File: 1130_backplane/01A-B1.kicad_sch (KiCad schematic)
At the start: 86 parts

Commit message: DN101-DN111 added to backplane schematics, DN111 01B-A1 connections made, 01B-B1 connections to be made when all signals on connectors
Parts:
- removed J100, J101, J102, J103, J104, J105, J106, J107, J108, J109, J110, J111, J112, J113, J114, J115, J116, J117, J118, J119, J120, J121, J122, J123, J124, J125, J126, J127, J128, J129, J130, J131, J132, J133, J134, J135, J136, J137, J138, J139, J140, J141, J142, J143, J144, J145, J146, J147, J148, J149, J150, J151, J152, J153, J154, J155, J156, J157, J158, J159, J160, J161, J162, J163, J164, J165, J166, J167, J168, J169, J170, J171, J172, J87, J88, J89, J90, J91, J92, J93, J94, J95, J96, J97, J98, J99: ~, symbol Connector_Generic:Conn_02x12_Row_Letter_First
- added J? (x86): ~, symbol Connector_Generic:Conn_02x12_Row_Letter_First
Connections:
- net +3V: now also J?.b2 (Pin_b2), J?.b2 (Pin_b2), J?.b2 (Pin_b2), J?.b2 (Pin_b2), J?.b2 (Pin_b2), J?.b2 (Pin_b2), J?.b2 (Pin_b2), J?.b2 (Pin_b2), J?.b2 (Pin_b2), J?.b2 (Pin_b2), J?.b2 (Pin_b2), J?.b2 (Pin_b2), J?.b2 (Pin_b2), J?.b2 (Pin_b2), J?.b2 (Pin_b2), J?.b2 (Pin_b2), J?.b2 (Pin_b2), J?.b2 (Pin_b2), J?.b2 (Pin_b2), J?.b2 (Pin_b2), J?.b2 (Pin_b2), J?.b2 (Pin_b2), J?.b2 (Pin_b2), J?.b2 (Pin_b2), J?.b2 (Pin_b2), J?.b2 (Pin_b2), J?.b2 (Pin_b2), J?.b2 (Pin_b2), J?.b2 (Pin_b2), J?.b2 (Pin_b2), J?.b2 (Pin_b2), J?.b2 (Pin_b2), J?.b2 (Pin_b2), J?.b2 (Pin_b2), J?.b2 (Pin_b2), J?.b2 (Pin_b2), J?.b2 (Pin_b2), J?.b2 (Pin_b2), J?.b2 (Pin_b2), J?.b2 (Pin_b2), J?.b2 (Pin_b2), J?.b2 (Pin_b2), J?.b2 (Pin_b2), J?.b2 (Pin_b2), J?.b2 (Pin_b2), J?.b2 (Pin_b2), J?.b2 (Pin_b2), J?.b2 (Pin_b2), J?.b2 (Pin_b2), J?.b2 (Pin_b2), J?.b2 (Pin_b2), J?.b2 (Pin_b2), J?.b2 (Pin_b2), J?.b2 (Pin_b2), J?.b2 (Pin_b2), J?.b2 (Pin_b2), J?.b2 (Pin_b2), J?.b2 (Pin_b2), J?.b2 (Pin_b2), J?.b2 (Pin_b2), J?.b2 (Pin_b2), J?.b2 (Pin_b2), J?.b2 (Pin_b2), J?.b2 (Pin_b2), J?.b2 (Pin_b2), J?.b2 (Pin_b2), J?.b2 (Pin_b2), J?.b2 (Pin_b2), J?.b2 (Pin_b2), J?.b2 (Pin_b2), J?.b2 (Pin_b2), J?.b2 (Pin_b2), J?.b2 (Pin_b2), J?.b2 (Pin_b2), J?.b2 (Pin_b2), J?.b2 (Pin_b2), J?.b2 (Pin_b2)
- net +6V: now also J?.a10 (Pin_a10), J?.a10 (Pin_a10), J?.a10 (Pin_a10), J?.a10 (Pin_a10), J?.a10 (Pin_a10), J?.a10 (Pin_a10), J?.a10 (Pin_a10), J?.a10 (Pin_a10), J?.a10 (Pin_a10), J?.a10 (Pin_a10), J?.a10 (Pin_a10), J?.a10 (Pin_a10), J?.a10 (Pin_a10), J?.a10 (Pin_a10), J?.a10 (Pin_a10), J?.a10 (Pin_a10), J?.a10 (Pin_a10), J?.a10 (Pin_a10), J?.a10 (Pin_a10), J?.a10 (Pin_a10), J?.a10 (Pin_a10), J?.a10 (Pin_a10), J?.a10 (Pin_a10), J?.a10 (Pin_a10), J?.a10 (Pin_a10), J?.a10 (Pin_a10), J?.a10 (Pin_a10), J?.a10 (Pin_a10), J?.a10 (Pin_a10), J?.a10 (Pin_a10), J?.a10 (Pin_a10), J?.a10 (Pin_a10), J?.a10 (Pin_a10), J?.a10 (Pin_a10), J?.a10 (Pin_a10), J?.a10 (Pin_a10), J?.a10 (Pin_a10), J?.a10 (Pin_a10), J?.a10 (Pin_a10), J?.a10 (Pin_a10), J?.a10 (Pin_a10), J?.a10 (Pin_a10), J?.a10 (Pin_a10), J?.a10 (Pin_a10), J?.a10 (Pin_a10), J?.a10 (Pin_a10), J?.a10 (Pin_a10), J?.a10 (Pin_a10), J?.a10 (Pin_a10), J?.a10 (Pin_a10), J?.a10 (Pin_a10), J?.a10 (Pin_a10), J?.a10 (Pin_a10), J?.a10 (Pin_a10), J?.a10 (Pin_a10), J?.a10 (Pin_a10), J?.a10 (Pin_a10), J?.a10 (Pin_a10), J?.a10 (Pin_a10), J?.a10 (Pin_a10), J?.a10 (Pin_a10), J?.a10 (Pin_a10), J?.a10 (Pin_a10), J?.a10 (Pin_a10), J?.a10 (Pin_a10), J?.a10 (Pin_a10), J?.a10 (Pin_a10), J?.a10 (Pin_a10), J?.a10 (Pin_a10), J?.a10 (Pin_a10), J?.a10 (Pin_a10), J?.a10 (Pin_a10), J?.a10 (Pin_a10), J?.a10 (Pin_a10), J?.a10 (Pin_a10), J?.a10 (Pin_a10), J?.a10 (Pin_a10)
- net -3V: now also J?.a5 (Pin_a5), J?.a5 (Pin_a5), J?.a5 (Pin_a5), J?.a5 (Pin_a5), J?.a5 (Pin_a5), J?.a5 (Pin_a5), J?.a5 (Pin_a5), J?.a5 (Pin_a5), J?.a5 (Pin_a5), J?.a5 (Pin_a5), J?.a5 (Pin_a5), J?.a5 (Pin_a5), J?.a5 (Pin_a5), J?.a5 (Pin_a5), J?.a5 (Pin_a5), J?.a5 (Pin_a5), J?.a5 (Pin_a5), J?.a5 (Pin_a5), J?.a5 (Pin_a5), J?.a5 (Pin_a5), J?.a5 (Pin_a5), J?.a5 (Pin_a5), J?.a5 (Pin_a5), J?.a5 (Pin_a5), J?.a5 (Pin_a5), J?.a5 (Pin_a5), J?.a5 (Pin_a5), J?.a5 (Pin_a5), J?.a5 (Pin_a5), J?.a5 (Pin_a5), J?.a5 (Pin_a5), J?.a5 (Pin_a5), J?.a5 (Pin_a5), J?.a5 (Pin_a5), J?.a5 (Pin_a5), J?.a5 (Pin_a5), J?.a5 (Pin_a5), J?.a5 (Pin_a5), J?.a5 (Pin_a5), J?.a5 (Pin_a5), J?.a5 (Pin_a5), J?.a5 (Pin_a5), J?.a5 (Pin_a5), J?.a5 (Pin_a5), J?.a5 (Pin_a5), J?.a5 (Pin_a5), J?.a5 (Pin_a5), J?.a5 (Pin_a5), J?.a5 (Pin_a5), J?.a5 (Pin_a5), J?.a5 (Pin_a5), J?.a5 (Pin_a5), J?.a5 (Pin_a5), J?.a5 (Pin_a5), J?.a5 (Pin_a5), J?.a5 (Pin_a5), J?.a5 (Pin_a5), J?.a5 (Pin_a5), J?.a5 (Pin_a5), J?.a5 (Pin_a5), J?.a5 (Pin_a5), J?.a5 (Pin_a5), J?.a5 (Pin_a5), J?.a5 (Pin_a5), J?.a5 (Pin_a5), J?.a5 (Pin_a5), J?.a5 (Pin_a5), J?.a5 (Pin_a5), J?.a5 (Pin_a5), J?.a5 (Pin_a5), J?.a5 (Pin_a5), J?.a5 (Pin_a5), J?.a5 (Pin_a5), J?.a5 (Pin_a5), J?.a5 (Pin_a5), J?.a5 (Pin_a5), J?.a5 (Pin_a5)
- net -IO_BIT_0: now also J?.a2 (Pin_a2), J?.a2 (Pin_a2)
- net -IO_BIT_1: now also J?.b1 (Pin_b1), J?.b1 (Pin_b1)
- net -IO_BIT_10: now also J?.a7 (Pin_a7), J?.a7 (Pin_a7)
- net -IO_BIT_11: now also J?.b6 (Pin_b6), J?.b6 (Pin_b6)
- net -IO_BIT_12: now also J?.a8 (Pin_a8), J?.a8 (Pin_a8)
- net -IO_BIT_13: now also J?.b8 (Pin_b8), J?.b8 (Pin_b8)
- net -IO_BIT_14: now also J?.a9 (Pin_a9), J?.a9 (Pin_a9)
- net -IO_BIT_15: now also J?.b9 (Pin_b9), J?.b9 (Pin_b9)
- net -IO_BIT_2: now also J?.a3 (Pin_a3), J?.a3 (Pin_a3)
- net -IO_BIT_3: now also J?.a1 (Pin_a1), J?.b2 (Pin_b2), J?.b2 (Pin_b2)
- net -IO_BIT_4: now also J?.a4 (Pin_a4), J?.a4 (Pin_a4)
- net -IO_BIT_5: now also J?.b3 (Pin_b3), J?.b3 (Pin_b3)
- net -IO_BIT_6: now also J?.a11 (Pin_a11), J?.a5 (Pin_a5), J?.a5 (Pin_a5)
- net -IO_BIT_7: now also J?.b4 (Pin_b4), J?.b4 (Pin_b4)
- net -IO_BIT_8: now also J?.a6 (Pin_a6), J?.a6 (Pin_a6)
- net -IO_BIT_9: now also J?.b5 (Pin_b5), J?.b5 (Pin_b5)
- net GND: now also J?.b7 (Pin_b7), J?.b7 (Pin_b7), J?.b7 (Pin_b7), J?.b7 (Pin_b7), J?.b7 (Pin_b7), J?.b7 (Pin_b7), J?.b7 (Pin_b7), J?.b7 (Pin_b7), J?.b7 (Pin_b7), J?.b7 (Pin_b7), J?.b7 (Pin_b7), J?.b7 (Pin_b7), J?.b7 (Pin_b7), J?.b7 (Pin_b7), J?.b7 (Pin_b7), J?.b7 (Pin_b7), J?.b7 (Pin_b7), J?.b7 (Pin_b7), J?.b7 (Pin_b7), J?.b7 (Pin_b7), J?.b7 (Pin_b7), J?.b7 (Pin_b7), J?.b7 (Pin_b7), J?.b7 (Pin_b7), J?.b7 (Pin_b7), J?.b7 (Pin_b7), J?.b7 (Pin_b7), J?.b7 (Pin_b7), J?.b7 (Pin_b7), J?.b7 (Pin_b7), J?.b7 (Pin_b7), J?.b7 (Pin_b7), J?.b7 (Pin_b7), J?.b7 (Pin_b7), J?.b7 (Pin_b7), J?.b7 (Pin_b7), J?.b7 (Pin_b7), J?.b7 (Pin_b7), J?.b7 (Pin_b7), J?.b7 (Pin_b7), J?.b7 (Pin_b7), J?.b7 (Pin_b7), J?.b7 (Pin_b7), J?.b7 (Pin_b7), J?.b7 (Pin_b7), J?.b7 (Pin_b7), J?.b7 (Pin_b7), J?.b7 (Pin_b7), J?.b7 (Pin_b7), J?.b7 (Pin_b7), J?.b7 (Pin_b7), J?.b7 (Pin_b7), J?.b7 (Pin_b7), J?.b7 (Pin_b7), J?.b7 (Pin_b7), J?.b7 (Pin_b7), J?.b7 (Pin_b7), J?.b7 (Pin_b7), J?.b7 (Pin_b7), J?.b7 (Pin_b7), J?.b7 (Pin_b7), J?.b7 (Pin_b7), J?.b7 (Pin_b7), J?.b7 (Pin_b7), J?.b7 (Pin_b7), J?.b7 (Pin_b7), J?.b7 (Pin_b7), J?.b7 (Pin_b7), J?.b7 (Pin_b7), J?.b7 (Pin_b7), J?.b7 (Pin_b7), J?.b7 (Pin_b7), J?.b7 (Pin_b7), J?.b7 (Pin_b7), J?.b7 (Pin_b7), J?.b7 (Pin_b7), J?.b7 (Pin_b7), J?.b7 (Pin_b7), J?.b7 (Pin_b7), J?.b7 (Pin_b7), J?.b7 (Pin_b7), J?.b7 (Pin_b7), J?.b7 (Pin_b7), J?.b7 (Pin_b7), J?.b7 (Pin_b7), J?.b7 (Pin_b7)

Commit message: Add labels for cable runs, completed tracing for DN111 from previous commit, decided it would be too much work to go back and route later... Completed DN201 page.
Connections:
- net +3V: no longer J?.b2 (Pin_b2)
- net +6V: no longer J?.a10 (Pin_a10)
- net -3V: no longer J?.a5 (Pin_a5)
- net +INT_RUN_MODE: now reaches J?.a4 (Pin_a4)
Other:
- note added: "CABL 01A-A1N2"
- note added: "CABL 01A-C1T1"
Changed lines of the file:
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@@
     (stroke (width 0) (type solid) (color 0 0 0 0))
-  )
-  (wire (pts (xy 787.4 306.07) (xy 795.02 306.07))
-    (stroke (width 0) (type default) (color 0 0 0 0))
   )
   (polyline (pts (xy 34.29 72.39) (xy 35.56 72.39))
@@
     (stroke (width 0) (type default) (color 0 0 0 0))
   )
-  (wire (pts (xy 787.4 318.77) (xy 795.02 318.77))
-    (stroke (width 0) (type default) (color 0 0 0 0))
-  )
   (wire (pts (xy 744.22 298.45) (xy 751.84 298.45))
     (stroke (width 0) (type default) (color 0 0 0 0))
@@
     (stroke (width 0) (type default) (color 0 0 0 0))
   )
-  (wire (pts (xy 807.72 298.45) (xy 815.34 298.45))
-    (stroke (width 0) (type default) (color 0 0 0 0))
-  )
   (polyline (pts (xy 308.61 30.48) (xy 308.61 29.21))
     (stroke (width 0) (type solid) (color 0 0 0 0))
@@
     (effects (font (size 5 5) (thickness 1) bold) (justify left bottom))
   )
+  (text "CABL 01A-C1T1" (at 355.6 25.4 0)
+    (effects (font (size 1.27 1.27)) (justify left bottom))
+  )
   (text "D" (at 312.42 39.37 0)
     (effects (font (size 1.27 1.27)) (justify left bottom))
@@
     (effects (font (size 1.27 1.27)) (justify left bottom))
   )
+  (text "CABL 01A-A1N2" (at 31.75 102.87 0)
+    (effects (font (size 1.27 1.27)) (justify left bottom))
+  )
   (text "F" (at 354.33 91.44 0)
     (effects (font (size 5 5) (thickness 1) bold) (justify left bottom))
@@
     (effects (font (size 1.27 1.27)) (justify left bottom))
   )
-  (label "-3V" (at 787.4 306.07 180)
-    (effects (font (size 1.27 1.27)) (justify right bottom))
-  )
   (label "+6V" (at 596.9 204.47 180)
     (effects (font (size 1.27 1.27)) (justify right bottom))
@@
     (effects (font (size 1.27 1.27)) (justify right bottom))
   )
-  (label "+6V" (at 787.4 318.77 180)
-    (effects (font (size 1.27 1.27)) (justify right bottom))
-  )
   (label "-3V" (at 533.4 153.67 180)
     (effects (font (size 1.27 1.27)) (justify right bottom))
@@
     (effects (font (size 1.27 1.27)) (justify right bottom))
   )
-  (label "+3V" (at 815.34 298.45 0)
-    (effects (font (size 1.27 1.27)) (justify left bottom))
+  (label "+INT_RUN_MODE" (at 795.02 303.53 180)
+    (effects (font (size 1.27 1.27)) (justify right bottom))
   )
   (label "+3V" (at 688.34 222.25 0)

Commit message: Add labels for bottom T[x] connectors, finished page DU101.
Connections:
- net +3V: no longer J?.b2 (Pin_b2)
- net +6V: no longer J?.a10 (Pin_a10)
- net -3V: no longer J?.a5 (Pin_a5)
- net +U_REG_8_PWR: now reaches J?.a11 (Pin_a11)
- net +U_REG_8_PWR: now also J?.b8 (Pin_b8)
- net +U_REG_9_PWR: now reaches J?.a12 (Pin_a12)
- net +U_REG_9_PWR: now also J?.b9 (Pin_b9)
- net +XIO_CONTROL: now reaches J?.a1 (Pin_a1)
- net +XIO_CONTROL: now also J?.a5 (Pin_a5), J?.a8 (Pin_a8)
- net +XIO_READ: now reaches J?.a3 (Pin_a3)
- net +XIO_READ: now also J?.a7 (Pin_a7)
- net +XIO_START_READ: now reaches J?.a4 (Pin_a4)
- net +XIO_WRITE: now reaches J?.b3 (Pin_b3)
- net +XIO_START_WRITE: now reaches J?.b4 (Pin_b4)
- net +XIO_SENSE_DEVICE: now reaches J?.b5 (Pin_b5)
- net +XIO_SENSE_DEVICE: now also J?.b9 (Pin_b9)
- net +XIO_SENSE_ILSW: now reaches J?.b6 (Pin_b6)
- net +XIO_SENSE_ILSW: now also J?.a3 (Pin_a3)
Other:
- note added: "CABL 01A-A1N5"
- note added: "CABL 01A-A1T6"
- note added: "CABL 01A-C1T2"
- moved on the sheet: J?

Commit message: Fix routing mistake from DU101 for T6, was 01A-A1 to 01A-B1, corrected from 01A-A1 to 01A-C1, finished page DU111.
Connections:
- net +XIO_SENSE_ILSW: no longer J?.a3 (Pin_a3)
- net +U_REG_13_PWR: now reaches J?.b10 (Pin_b10)
- net +U_REG_13_PWR: now also J?.b10 (Pin_b10)
- net +U_REG_14_PWR: now reaches J?.b11 (Pin_b11)
- net +U_REG_14_PWR: now also J?.b11 (Pin_b11)
- net +U_REG_15_PWR: now reaches J?.b12 (Pin_b12)
- net +U_REG_15_PWR: now also J?.b12 (Pin_b12)
- net +AREA_6: now reaches J?.a11 (Pin_a11)
- net +AREA_6: now also J?.a2 (Pin_a2)
- net -XIO_SENSE_RESET_14: now reaches J?.a2 (Pin_a2)
- net +AREA_2: now reaches J?.a6 (Pin_a6)
- net +AREA_3: now reaches J?.a7 (Pin_a7)
- net +XIO_SENSE_RESET_15: now reaches J?.a8 (Pin_a8)
- net +XIO_SENSE_RESET_15: now also J?.b10 (Pin_b10)
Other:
- note removed: "CABL 01A-A1T6"
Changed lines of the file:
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@@
     (effects (font (size 5 5) (thickness 1) bold) (justify left bottom))
-  )
-  (text "CABL 01A-A1T6" (at 393.7 393.7 0)
-    (effects (font (size 1.27 1.27)) (justify left bottom))
   )
   (text "E" (at 327.66 368.3 0)
@@
     (effects (font (size 1.27 1.27)) (justify right bottom))
   )
+  (label "+U_REG_13_PWR" (at 45.72 127 0)
+    (effects (font (size 1.27 1.27)) (justify left bottom))
+  )
+  (label "-XIO_SENSE_RESET_14" (at 389.89 63.5 270)
+    (effects (font (size 1.27 1.27)) (justify right bottom))
+  )
   (label "-3V" (at 469.9 228.6 180)
     (effects (font (size 1.27 1.27)) (justify right bottom))
@@
     (effects (font (size 1.27 1.27)) (justify right bottom))
   )
+  (label "+XIO_SENSE_RESET_15" (at 45.72 241.3 0)
+    (effects (font (size 1.27 1.27)) (justify left bottom))
+  )
   (label "GND" (at 307.34 195.58 0)
     (effects (font (size 1.27 1.27)) (justify left bottom))
@@
     (effects (font (size 1.27 1.27)) (justify left bottom))
   )
-  (label "+XIO_SENSE_ILSW" (at 392.43 369.57 270)
+  (label "+AREA_2" (at 400.05 63.5 270)
     (effects (font (size 1.27 1.27)) (justify right bottom))
   )
@@
     (effects (font (size 1.27 1.27)) (justify left bottom))
   )
+  (label "+U_REG_14_PWR" (at 45.72 129.54 0)
+    (effects (font (size 1.27 1.27)) (justify left bottom))
+  )
   (label "GND" (at 434.34 195.58 0)
     (effects (font (size 1.27 1.27)) (justify left bottom))
@@
     (effects (font (size 1.27 1.27)) (justify left bottom))
   )
+  (label "+AREA_6" (at 412.75 63.5 270)
+    (effects (font (size 1.27 1.27)) (justify right bottom))
+  )
   (label "GND" (at 370.84 157.48 0)
     (effects (font (size 1.27 1.27)) (justify left bottom))
@@
     (effects (font (size 1.27 1.27)) (justify left bottom))
   )
+  (label "+AREA_6" (at 33.02 220.98 180)
+    (effects (font (size 1.27 1.27)) (justify right bottom))
+  )
   (label "+6V" (at 342.9 317.5 180)
     (effects (font (size 1.27 1.27)) (justify right bottom))
@@
     (effects (font (size 1.27 1.27)) (justify right bottom))
   )
+  (label "+U_REG_14_PWR" (at 412.75 50.8 90)
+    (effects (font (size 1.27 1.27)) (justify left bottom))
+  )
   (label "+3V" (at 243.84 106.68 0)
     (effects (font (size 1.27 1.27)) (justify left bottom))
@@
     (effects (font (size 1.27 1.27)) (justify right bottom))
   )
+  (label "+U_REG_15_PWR" (at 45.72 132.08 0)
+    (effects (font (size 1.27 1.27)) (justify left bottom))
+  )
   (label "-3V" (at 342.9 228.6 180)
     (effects (font (size 1.27 1.27)) (justify right bottom))
@@
     (effects (font (size 1.27 1.27)) (justify right bottom))
   )
+  (label "+AREA_3" (at 402.59 63.5 270)
+    (effects (font (size 1.27 1.27)) (justify right bottom))
+  )
   (label "GND" (at 624.84 271.78 0)
     (effects (font (size 1.27 1.27)) (justify left bottom))
@@
     (effects (font (size 1.27 1.27)) (justify left bottom))
   )
+  (label "+U_REG_15_PWR" (at 415.29 50.8 90)
+    (effects (font (size 1.27 1.27)) (justify left bottom))
+  )
   (label "+3V" (at 180.34 297.18 0)
     (effects (font (size 1.27 1.27)) (justify left bottom))
@@
     (effects (font (size 1.27 1.27)) (justify left bottom))
   )
+  (label "+XIO_SENSE_RESET_15" (at 405.13 63.5 270)
+    (effects (font (size 1.27 1.27)) (justify right bottom))
+  )
   (label "-3V" (at 660.4 304.8 180)
     (effects (font (size 1.27 1.27)) (justify right bottom))
@@
     (effects (font (size 1.27 1.27)) (justify left bottom))
   )
+  (label "+U_REG_13_PWR" (at 410.21 50.8 90)
+    (effects (font (size 1.27 1.27)) (justify left bottom))
+  )

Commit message: Finish page KA101-KA111
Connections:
- net -DC_RESET_3: now reaches J?.a9 (Pin_a9)
- net -DC_RESET_3: now also J?.a9 (Pin_a9)
- net +PHASE_B: now reaches J?.b11 (Pin_b11)
- net +PHASE_B: now also J?.b11 (Pin_b11)
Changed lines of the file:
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@@
     (effects (font (size 1.27 1.27)) (justify left bottom))
+  )
+  (label "-DC_RESET_3" (at 795.02 314.96 180)
+    (effects (font (size 1.27 1.27)) (justify right bottom))
   )
   (label "+3V" (at 180.34 297.18 0)
@@
     (effects (font (size 1.27 1.27)) (justify right bottom))
   )
+  (label "-DC_RESET_3" (at 33.02 238.76 180)
+    (effects (font (size 1.27 1.27)) (justify right bottom))
+  )
+  (label "+PHASE_B" (at 45.72 243.84 0)
+    (effects (font (size 1.27 1.27)) (justify left bottom))
+  )
   (label "+3V" (at 370.84 144.78 0)
     (effects (font (size 1.27 1.27)) (justify left bottom))
@@
     (effects (font (size 1.27 1.27)) (justify right bottom))
   )
+  (label "+PHASE_B" (at 807.72 320.04 0)
+    (effects (font (size 1.27 1.27)) (justify left bottom))
+  )
   (label "+3V" (at 497.84 106.68 0)

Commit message: Redo annotations...
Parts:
- gave numbers to parts that had none: 86

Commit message: Finish page KM301-KM321
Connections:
- net +PRINTER_LVL_1_INTERRUPT_REQ: now reaches J87.a10 (Pin_a10)
- net +PRINTER_LVL_1_INTERRUPT_REQ: now also J125.a12 (Pin_a12)
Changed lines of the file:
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@@
+    (effects (font (size 1.27 1.27)) (justify right bottom))
+  )
+  (label "+PRINTER_LVL_1_INTERRUPT_REQ" (at 33.02 127 180)
     (effects (font (size 1.27 1.27)) (justify right bottom))
   )
@@
     (effects (font (size 1.27 1.27)) (justify left bottom))
   )
+  (label "+PRINTER_LVL_1_INTERRUPT_REQ" (at 415.29 63.5 270)
+    (effects (font (size 1.27 1.27)) (justify right bottom))
+  )
   (label "+6V" (at 406.4 317.5 180)

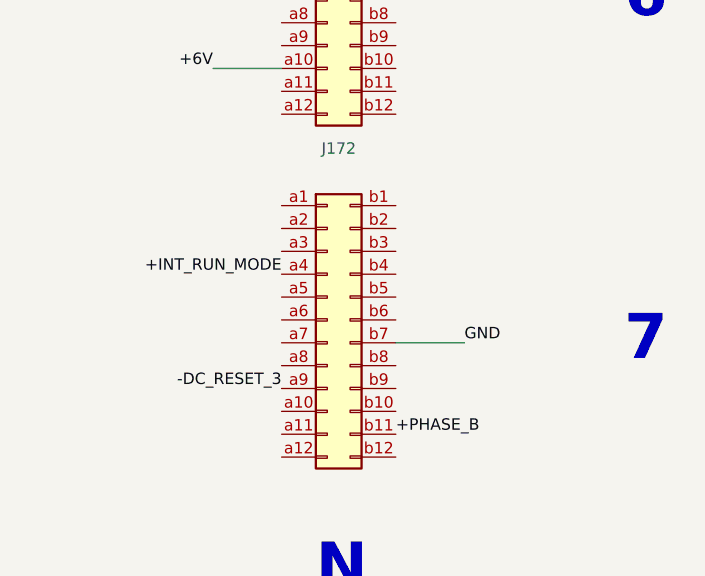
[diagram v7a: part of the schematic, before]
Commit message: Finish page KR101-KR111
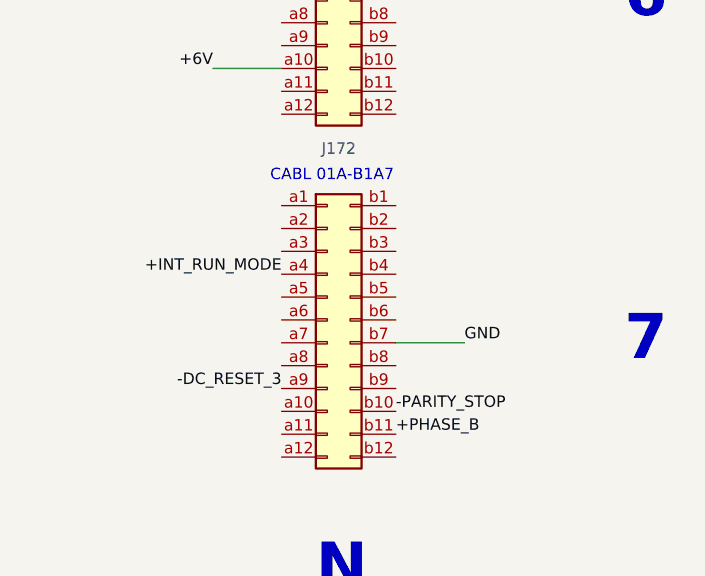
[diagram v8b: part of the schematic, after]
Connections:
- net -PARITY_STOP: now reaches J172.b10 (Pin_b10)
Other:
- note added: "CABL 01A-B1A7"
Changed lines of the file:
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@@
+    (effects (font (size 1.27 1.27)) (justify left bottom))
+  )
+  (text "CABL 01A-B1A7" (at 793.75 292.1 0)
     (effects (font (size 1.27 1.27)) (justify left bottom))
   )
@@
     (effects (font (size 1.27 1.27)) (justify left bottom))
   )
+  (label "-PARITY_STOP" (at 807.72 317.5 0)
+    (effects (font (size 1.27 1.27)) (justify left bottom))
+  )
